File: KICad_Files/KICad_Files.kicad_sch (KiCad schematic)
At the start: 48 parts, among them J1 Conn_01x03_MountingPin, J10 Conn_01x03_Pin, J2 USB_C_Receptacle_USB2.0_14P, J3 Conn_01x03_MountingPin, J4 Conn_01x03_MountingPin, J5 Conn_01x03_Pin, J6 Conn_01x06, J7 Conn_01x06, J8 Conn_01x03_Pin, J9 Conn_01x02_Pin, SW1 Reset, SW2 Boot, U1 ESP32-C3, U2 USBLC6-2SC6, U3 TPP361061-T6TR, Y1 40.0MHz

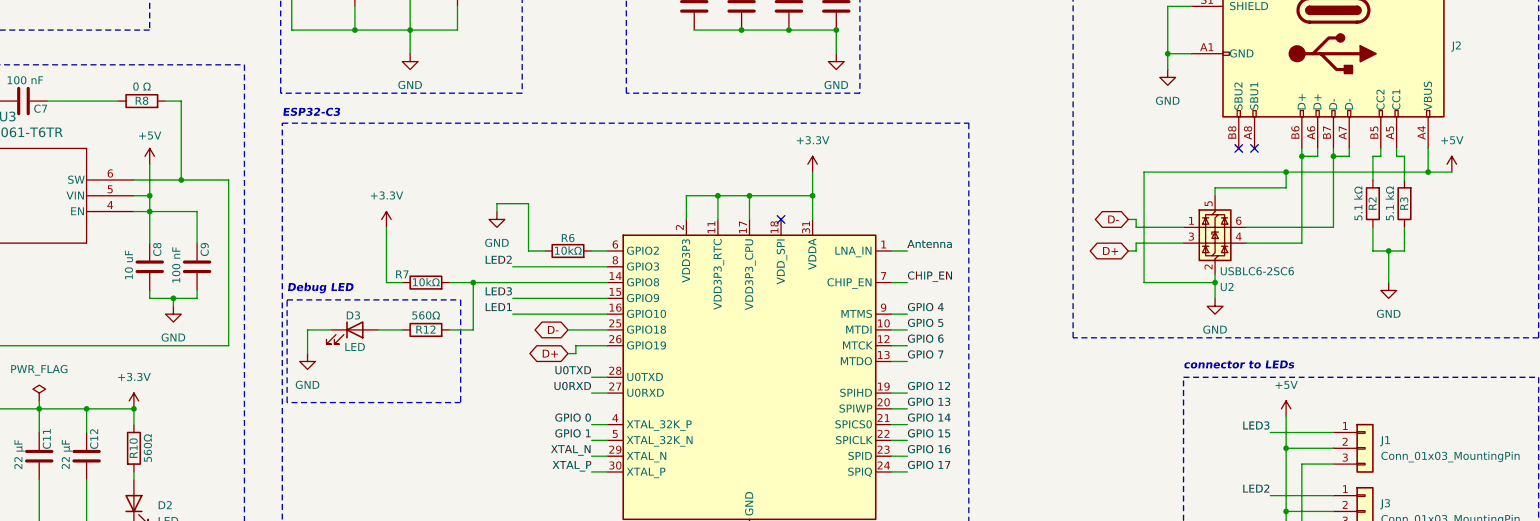
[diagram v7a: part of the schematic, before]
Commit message: Fixed ground connection to 5V error
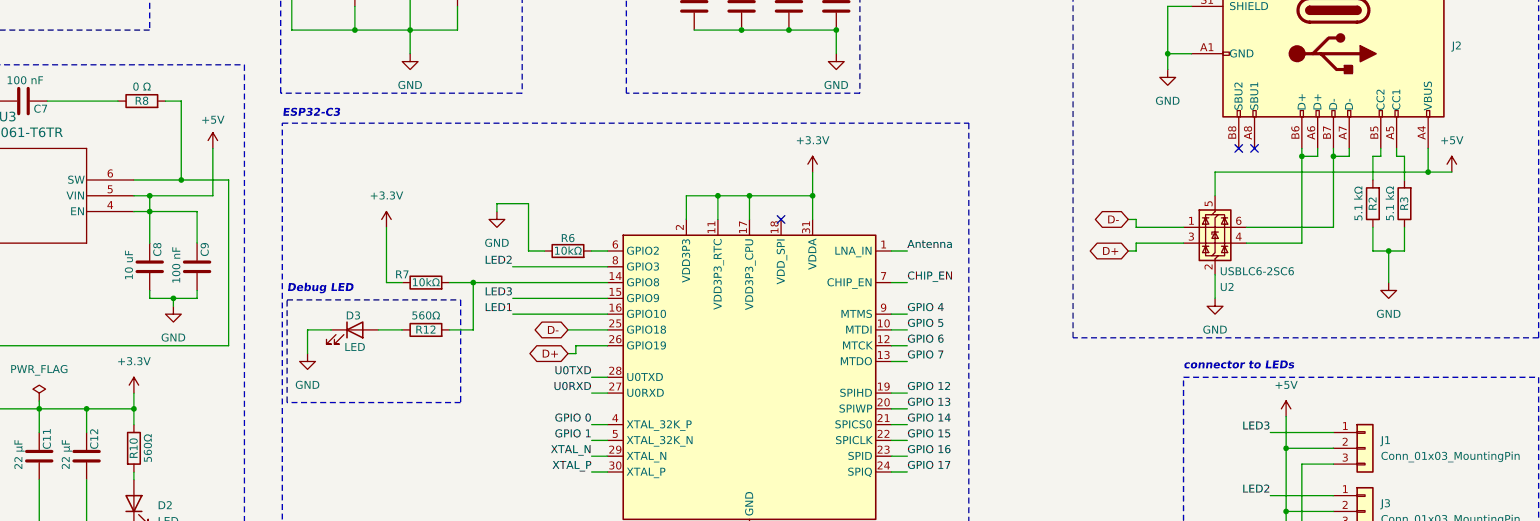
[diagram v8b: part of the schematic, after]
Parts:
- SW1, SW2: footprint Micro_button:Micro_button -> Micro_button:RKB2SJK250SMTR LFS
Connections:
- net +5V: no longer 26pF1.2, C1.2, C10.2, C11.1, C12.1, C13.2, C14.2, C2.2, C3.2, C4.2, C5.2, C6.2, C8.1, C9.1, D2.1 (K), D3.1 (K), J1.3 (Pin_3), J10.1 (Pin_1), J2.A1 (GND), J2.A12 (GND), J2.B1 (GND), J2.B12 (GND), J2.S1 (SHIELD), J3.3 (Pin_3), J4.3 (Pin_3), J6.6 (Pin_6), J7.6 (Pin_6), J9.2 (Pin_2), R11.1, R2.1, R3.1, R6.1, SW1.1, SW2.1, U1.33 (GND), U2.2 (GND), U3.2 (GND), Y1.2, Y1.4
- new net GND: 26pF1.2, C1.2, C10.2, C11.1, C12.1, C13.2, C14.2, C2.2, C3.2, C4.2, C5.2, C6.2, C8.1, C9.1, D2.1 (K), D3.1 (K), J1.3 (Pin_3), J10.1 (Pin_1), J2.A1 (GND), J2.A12 (GND), J2.B1 (GND), J2.B12 (GND), J2.S1 (SHIELD), J3.3 (Pin_3), J4.3 (Pin_3), J6.6 (Pin_6), J7.6 (Pin_6), J9.2 (Pin_2), R11.1, R2.1, R3.1, R6.1, SW1.1, SW2.1, U1.33 (GND), U2.2 (GND), U3.2 (GND), Y1.2, Y1.4
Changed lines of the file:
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@@
 	)
 	(junction
-		(at 346.71 157.48)
-		(diameter 0)
-		(color 0 0 0 0)
-	)
-	(junction
 		(at 349.25 35.56)
 		(diameter 0)
@@
 	)
 	(junction
-		(at 358.14 139.7)
-		(diameter 0)
-		(color 0 0 0 0)
-	)
-	(junction
 		(at 278.13 116.84)
 		(diameter 0)
@@
 	(wire
 		(pts
+			(xy 185.42 143.51) (xy 175.26 143.51)
+		)
+		(stroke
+			(width 0)
+			(type default)
+		)
+	)
+	(wire
+		(pts
 			(xy 365.76 137.16) (xy 365.76 148.59)
 		)
@@
 	(wire
 		(pts
-			(xy 346.71 142.24) (xy 346.71 143.51)
+			(xy 346.71 139.7) (xy 346.71 143.51)
 		)
 		(stroke
@@
 	(wire
 		(pts
-			(xy 335.28 139.7) (xy 358.14 139.7)
-		)
-		(stroke
-			(width 0)
-			(type default)
-		)
-	)
-	(wire
-		(pts
 			(xy 172.72 140.97) (xy 180.34 140.97)
 		)
@@
 	(wire
 		(pts
-			(xy 358.14 139.7) (xy 358.14 142.24)
-		)
-		(stroke
-			(width 0)
-			(type default)
-		)
-	)
-	(wire
-		(pts
 			(xy 213.36 157.48) (xy 215.9 157.48)
 		)
@@
 	(wire
 		(pts
-			(xy 346.71 157.48) (xy 346.71 156.21)
+			(xy 346.71 156.21) (xy 346.71 160.02)
 		)
 		(stroke
@@
 	(wire
 		(pts
-			(xy 346.71 142.24) (xy 358.14 142.24)
+			(xy 346.71 139.7) (xy 381 139.7)
 		)
 		(stroke
@@
 	(wire
 		(pts
-			(xy 335.28 139.7) (xy 335.28 157.48)
-		)
-		(stroke
-			(width 0)
-			(type default)
-		)
-	)
-	(wire
-		(pts
 			(xy 246.38 175.26) (xy 248.92 175.26)
 		)
@@
 	(wire
 		(pts
-			(xy 335.28 157.48) (xy 346.71 157.48)
-		)
-		(stroke
-			(width 0)
-			(type default)
-		)
-	)
-	(wire
-		(pts
 			(xy 294.64 180.34) (xy 297.18 180.34)
 		)
@@
 	(wire
 		(pts
-			(xy 346.71 160.02) (xy 346.71 157.48)
-		)
-		(stroke
-			(width 0)
-			(type default)
-		)
-	)
-	(wire
-		(pts
 			(xy 157.48 200.66) (xy 157.48 189.23)
 		)
@@
 	(wire
 		(pts
-			(xy 175.26 138.43) (xy 175.26 143.51)
+			(xy 185.42 135.89) (xy 185.42 143.51)
 		)
 		(stroke
@@
 	(wire
 		(pts
-			(xy 381 139.7) (xy 358.14 139.7)
-		)
-		(stroke
-			(width 0)
-			(type default)
-		)
-	)
-	(wire
-		(pts
 			(xy 382.27 88.9) (xy 387.35 88.9)
 		)
@@
 	(wire
 		(pts
+			(xy 172.72 175.26) (xy 172.72 177.8)
+		)
+		(stroke
+			(width 0)
+			(type default)
+		)
+	)
+	(wire
+		(pts
 			(xy 372.11 152.4) (xy 372.11 148.59)
 		)
@@
 	)
 	(symbol
+		(lib_id "power:GND")
+		(at 200.66 168.91 0)
+		(unit 1)
+		(exclude_from_sim no)
+		(in_bom yes)
+		(on_board yes)
+		(dnp no)
+		(fields_autoplaced yes)
+		(property "Reference" "#PWR28"
+			(at 200.66 175.26 0)
+			(effects
+				(font
+					(size 1.27 1.27)
+				)
+				(hide yes)
+			)
+		)
+		(property "Value" "GND"
+			(at 200.66 173.99 0)
+			(effects
+				(font
+					(size 1.27 1.27)
+				)
+			)
+		)
+		(property "Footprint" ""
+			(at 200.66 168.91 0)
+			(effects
+				(font
+					(size 1.27 1.27)
+				)
+				(hide yes)
+			)
+		)
+		(property "Datasheet" ""
+			(at 200.66 168.91 0)
+			(effects
+				(font
+					(size 1.27 1.27)
+				)
+				(hide yes)
+			)
+		)
+		(property "Description" "Power symbol creates a global label with name \"GND\" , ground"
+			(at 200.66 168.91 0)
+			(effects
+				(font
+					(size 1.27 1.27)
+				)
+				(hide yes)
+			)
+		)
+		(pin "1"
+		)
+		(instances
+			(project ""
+				(path "/34061aa1-1595-4a0a-9524-9b9b15681d54"
+					(reference "#PWR28")
+					(unit 1)
+				)
+			)
+		)
+	)
+	(symbol
 		(lib_id "power:+3.3V")
 		(at 281.94 139.7 0)
@@
 	(symbol
 		(lib_id "power:+5V")
-		(at 175.26 138.43 0)
+		(at 185.42 135.89 0)
 		(unit 1)
 		(exclude_from_sim no)
@@
 		(dnp no)
 		(property "Reference" "#PWR016"
-			(at 175.26 142.24 0)
+			(at 185.42 139.7 0)
 			(effects
 				(font
@@
 		)
 		(property "Value" "+5V"
-			(at 175.26 133.858 0)
+			(at 185.42 131.318 0)
 			(effects
 				(font
@@
 		)
 		(property "Footprint" ""
-			(at 175.26 138.43 0)
+			(at 185.42 135.89 0)
 			(effects
 				(font
@@
 		)
 		(property "Datasheet" ""
-			(at 175.26 138.43 0)
+			(at 185.42 135.89 0)
 			(effects
 				(font
@@
 		)
 		(property "Description" "Power symbol creates a global label with name \"+5V\""
-			(at 175.26 138.43 0)
+			(at 185.42 135.89 0)
 			(effects
 				(font
@@
 	)
 	(symbol
-		(lib_id "power:GND")
-		(at 200.66 168.91 0)
-		(unit 1)
-		(exclude_from_sim no)
-		(in_bom yes)
-		(on_board yes)
-		(dnp no)
-		(fields_autoplaced yes)
-		(property "Reference" "#PWR028"
-			(at 200.66 175.26 0)
-			(effects
-				(font
-					(size 1.27 1.27)
-				)
-				(hide yes)
-			)
-		)
-		(property "Value" "GND"
-			(at 200.66 173.99 0)
-			(effects
-				(font
-					(size 1.27 1.27)
-				)
-			)
-		)
-		(property "Footprint" ""
-			(at 200.66 168.91 0)
-			(effects
-				(font
-					(size 1.27 1.27)
-				)
-				(hide yes)
-			)
-		)
-		(property "Datasheet" ""
-			(at 200.66 168.91 0)
-			(effects
-				(font
-					(size 1.27 1.27)
-				)
-				(hide yes)
-			)
-		)
-		(property "Description" "Power symbol creates a global label with name \"GND\" , ground"
-			(at 200.66 168.91 0)
-			(effects
-				(font
-					(size 1.27 1.27)
-				)
-				(hide yes)
-			)
-		)
-		(pin "1"
-		)
-		(instances
-			(project "KICad_Files"
-				(path "/34061aa1-1595-4a0a-9524-9b9b15681d54"
-					(reference "#PWR028")
-					(unit 1)
-				)
-			)
-		)
-	)
-	(symbol
 		(lib_id "Switch:SW_Push")
 		(at 347.98 83.82 90)
@@
 			)
 		)
-		(property "Footprint" "Micro_button:Micro_button"
+		(property "Footprint" "Micro_button:RKB2SJK250SMTR LFS"
 			(at 342.9 83.82 0)
 			(effects
@@
 			)
 		)
-		(property "Datasheet" "~"
+		(property "Datasheet" "https://www.digikey.de/de/products/detail/c-k/RKB2SJK250SMTR-LFS/13997218"
 			(at 342.9 83.82 0)
 			(effects
@@
 			)
 		)
-		(property "Footprint" "Micro_button:Micro_button"
-			(at 372.11 83.82 0)
+		(property "Footprint" "Micro_button:RKB2SJK250SMTR LFS"
+			(at 373.126 84.074 0)
 			(effects
 				(font
@@
 			)
 		)
-		(property "Datasheet" "~"
+		(property "Datasheet" "https://www.digikey.de/de/products/detail/c-k/RKB2SJK250SMTR-LFS/13997218"
 			(at 372.11 83.82 0)
 			(effects
@@
 	(symbol
 		(lib_id "power:+3.3V")
-		(at 172.72 177.8 0)
+		(at 172.72 175.26 0)
 		(unit 1)
 		(exclude_from_sim no)
@@
 		(fields_autoplaced yes)
 		(property "Reference" "#PWR022"
-			(at 172.72 181.61 0)
+			(at 172.72 179.07 0)
 			(effects
 				(font
@@
 		)
 		(property "Value" "+3.3V"
-			(at 172.72 172.72 0)
+			(at 172.72 170.18 0)
 			(effects
 				(font
@@
 		)
 		(property "Footprint" ""
-			(at 172.72 177.8 0)
+			(at 172.72 175.26 0)
 			(effects
 				(font
@@
 		)
 		(property "Datasheet" ""
-			(at 172.72 177.8 0)
+			(at 172.72 175.26 0)
 			(effects
 				(font
@@
 		)
 		(property "Description" "Power symbol creates a global label with name \"+3.3V\""
-			(at 172.72 177.8 0)
+			(at 172.72 175.26 0)
 			(effects
 				(font
